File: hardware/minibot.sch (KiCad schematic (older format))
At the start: 36 parts, among them J1 USB_OTG, J2 SWD, J3 RESET, J4 BAUD, J5 CONN_01X18, SW1 BOOT, SW2 RESET, U1 TLV70233DBV, U6 RN41, U7 LSM6DS3US

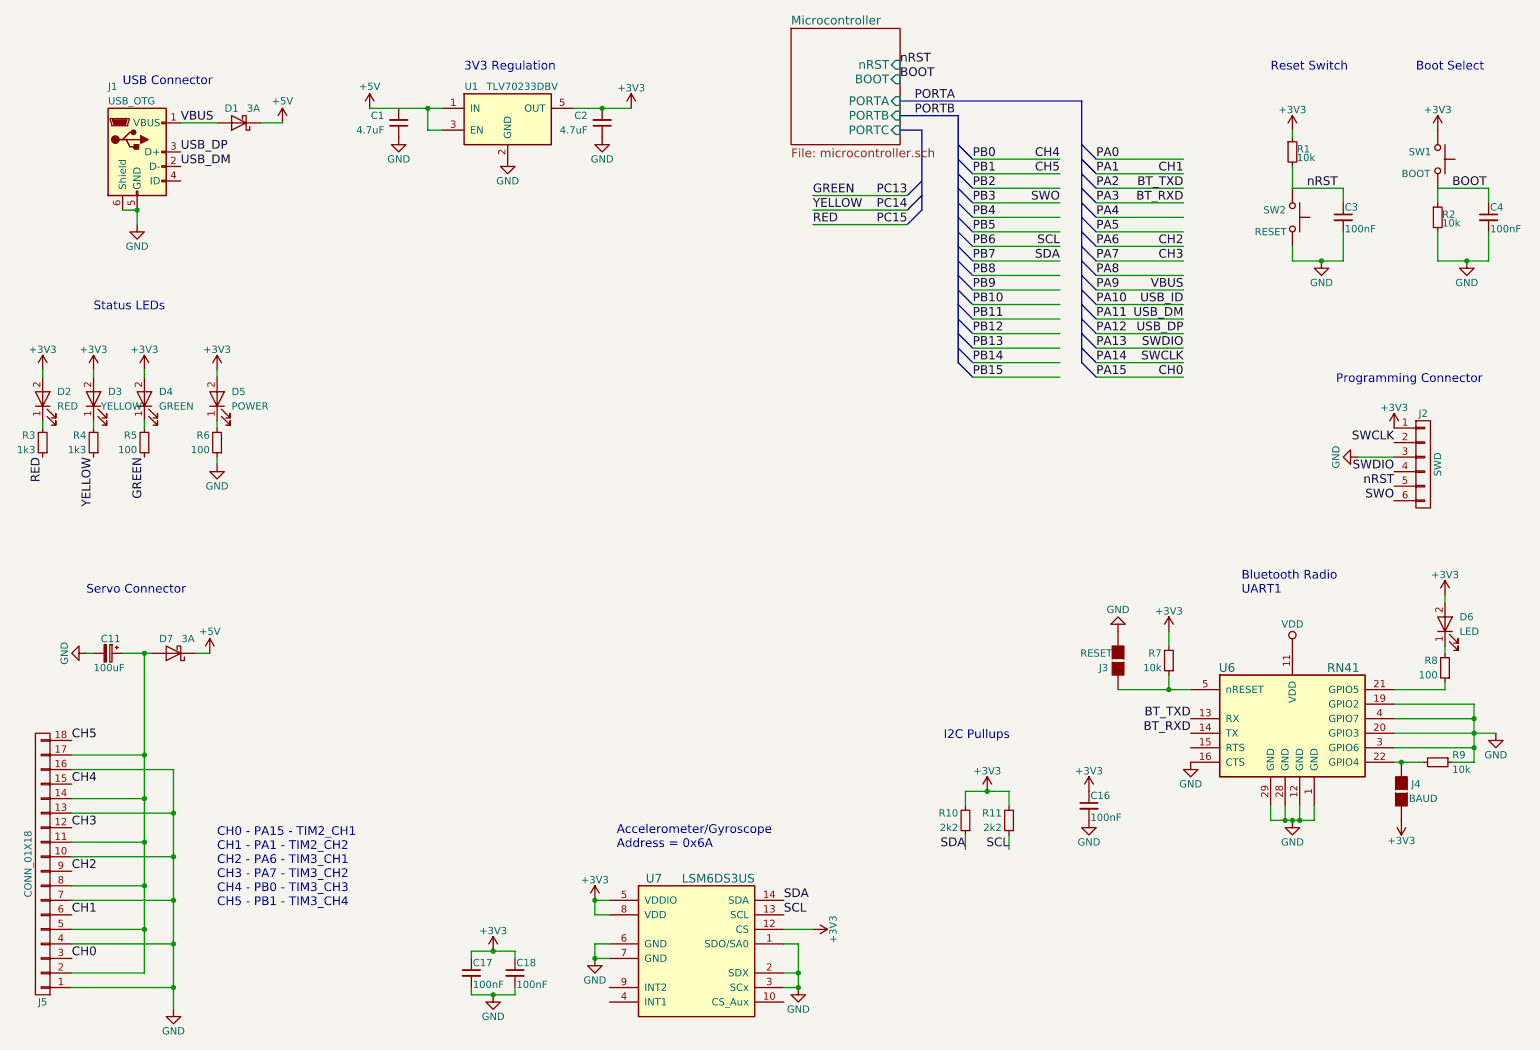
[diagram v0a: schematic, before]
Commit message: Start laying out the components for the PCB
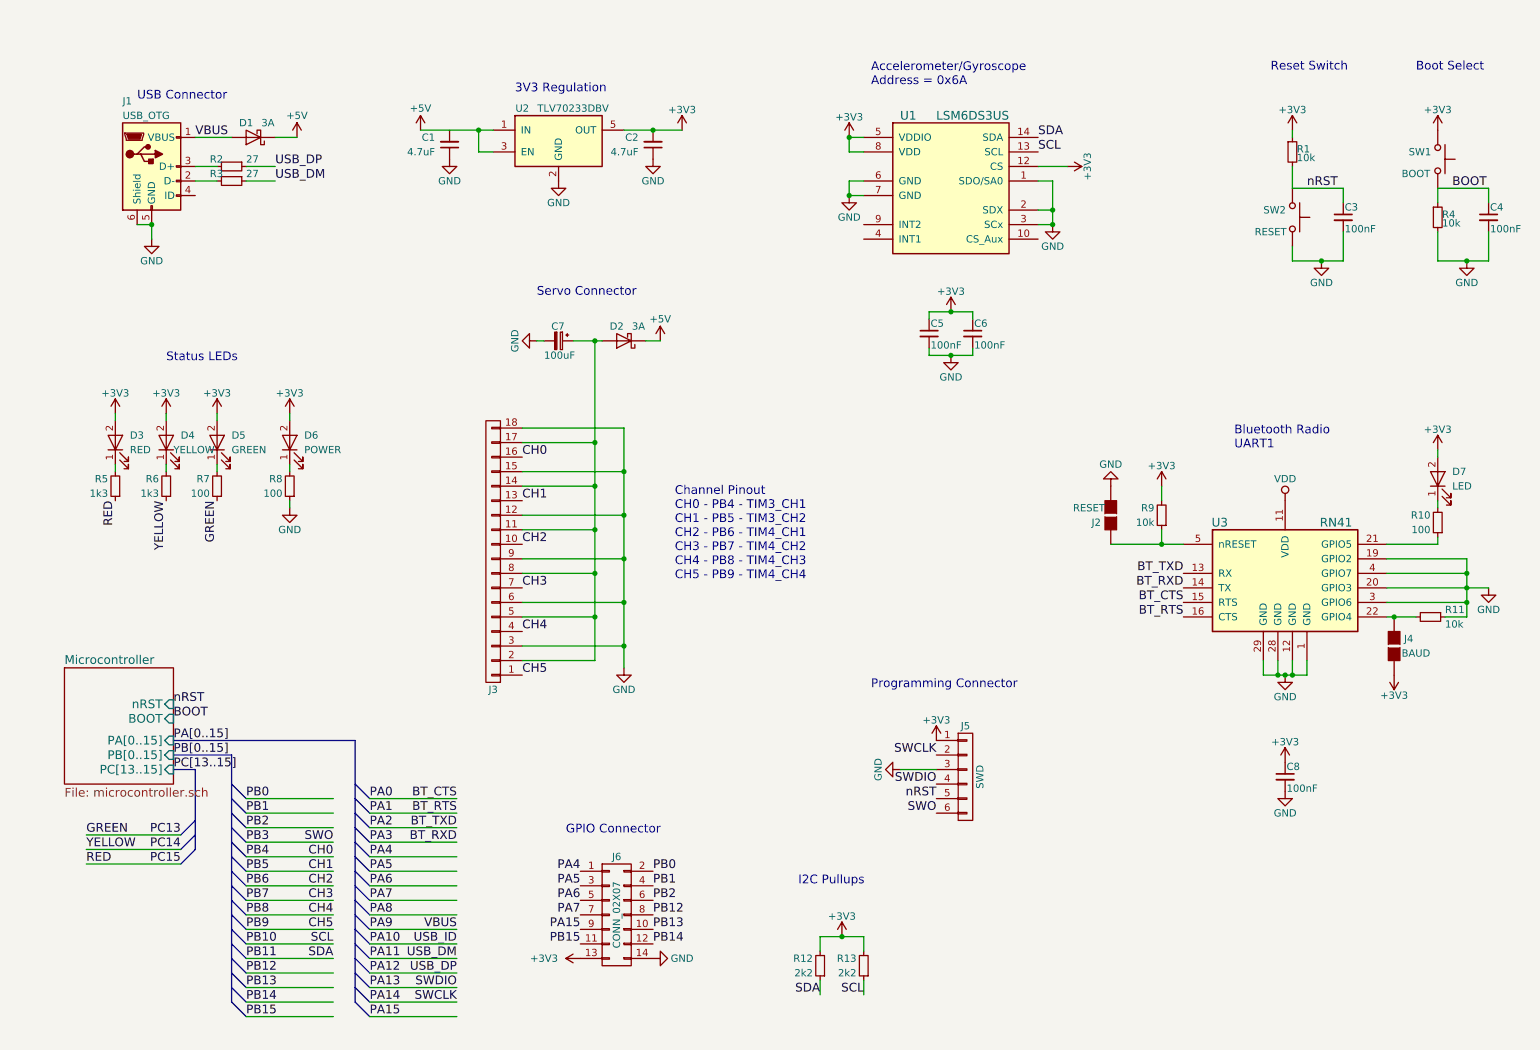
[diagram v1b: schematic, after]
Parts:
- added J6: CONN_02X07, Pin_Headers:Pin_Header_Straight_2x07_Pitch1.27mm, symbol CONN_02X07
- added R2, R3: 27, Resistors_SMD:R_0603, symbol R_Small
- J3: renamed from J5; footprint (none) -> modules:Pin_Header_Angled_3x06_Pitch2.54mm
- J5: renamed from J2; footprint Pin_Headers:Pin_Header_Angled_1x06_Pitch1.27mm -> Pin_Headers:Pin_Header_Straight_1x06_Pitch1.27mm
- SW1, SW2: footprint (none) -> Buttons_Switches_SMD:Panasonic_EVQPUK_EVQPUB
- U1: renamed from U7; footprint (none) -> modules:LSM6DS3US
- U3: renamed from U6; footprint (none) -> modules:RN41
- renumbered C17 to C5, C18 to C6, C11 to C7, C16 to C8, D7 to D2, D2 to D3, D3 to D4, D4 to D5, D5 to D6, D6 to D7, J3 to J2, R8 to R10, R9 to R11, R10 to R12, R11 to R13, R2 to R4, R3 to R5, R4 to R6, R5 to R7, R6 to R8, R7 to R9, U1 to U2
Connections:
- net labels added: BT_CTS, BT_RTS, PA[0..15], PB[0..15], PC[13..15]
- net labels removed: PORTA, PORTB
- wire segments 125 -> 129
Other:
- note added: "Channel Pinout\nCH0 - PB4 - TIM3_CH1\nCH1 - PB5 - TIM3_CH2\nCH2 - PB6 - TIM4_CH1\nCH3 - PB7 - TIM4_CH2\nCH4 - PB8 - TIM4_CH3\nCH5 - PB9 - TIM4_CH4"
- note added: "GPIO Connector\n"
- note removed: "CH0 - PA15 - TIM2_CH1\nCH1 - PA1 - TIM2_CH2\nCH2 - PA6 - TIM3_CH1\nCH3 - PA7 - TIM3_CH2\nCH4 - PB0 - TIM3_CH3\nCH5 - PB1 - TIM3_CH4"
- moved on the sheet: C1, C2, C5, C6, C7, C8, D1, D2, D3, D4, D5, D6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

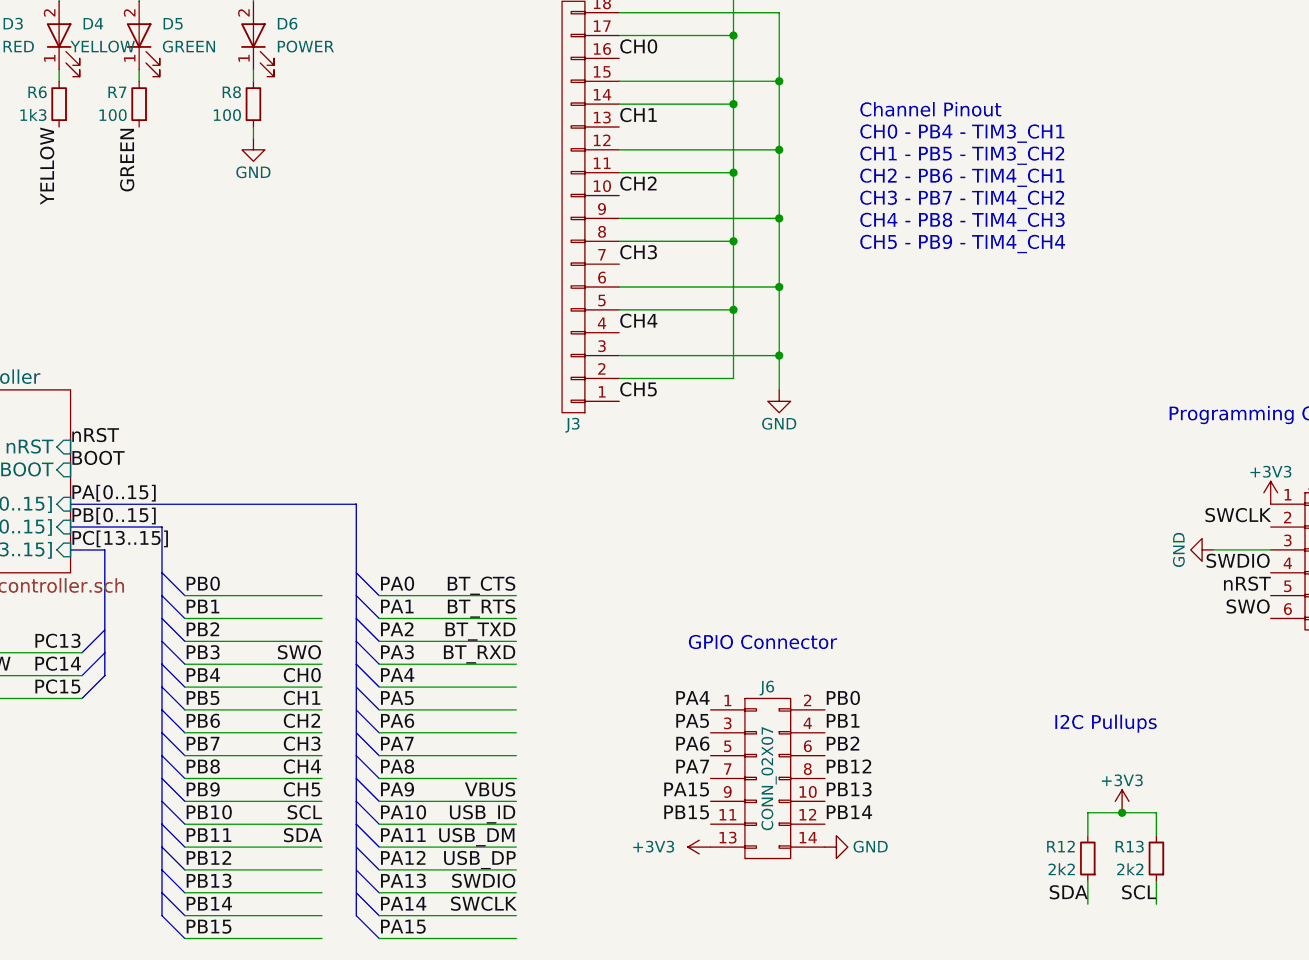
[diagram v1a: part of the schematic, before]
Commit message: Modify the schematic and PCB. At this stage the pinout should be considered and very careful selection of which peripheral goes where needs to be done.
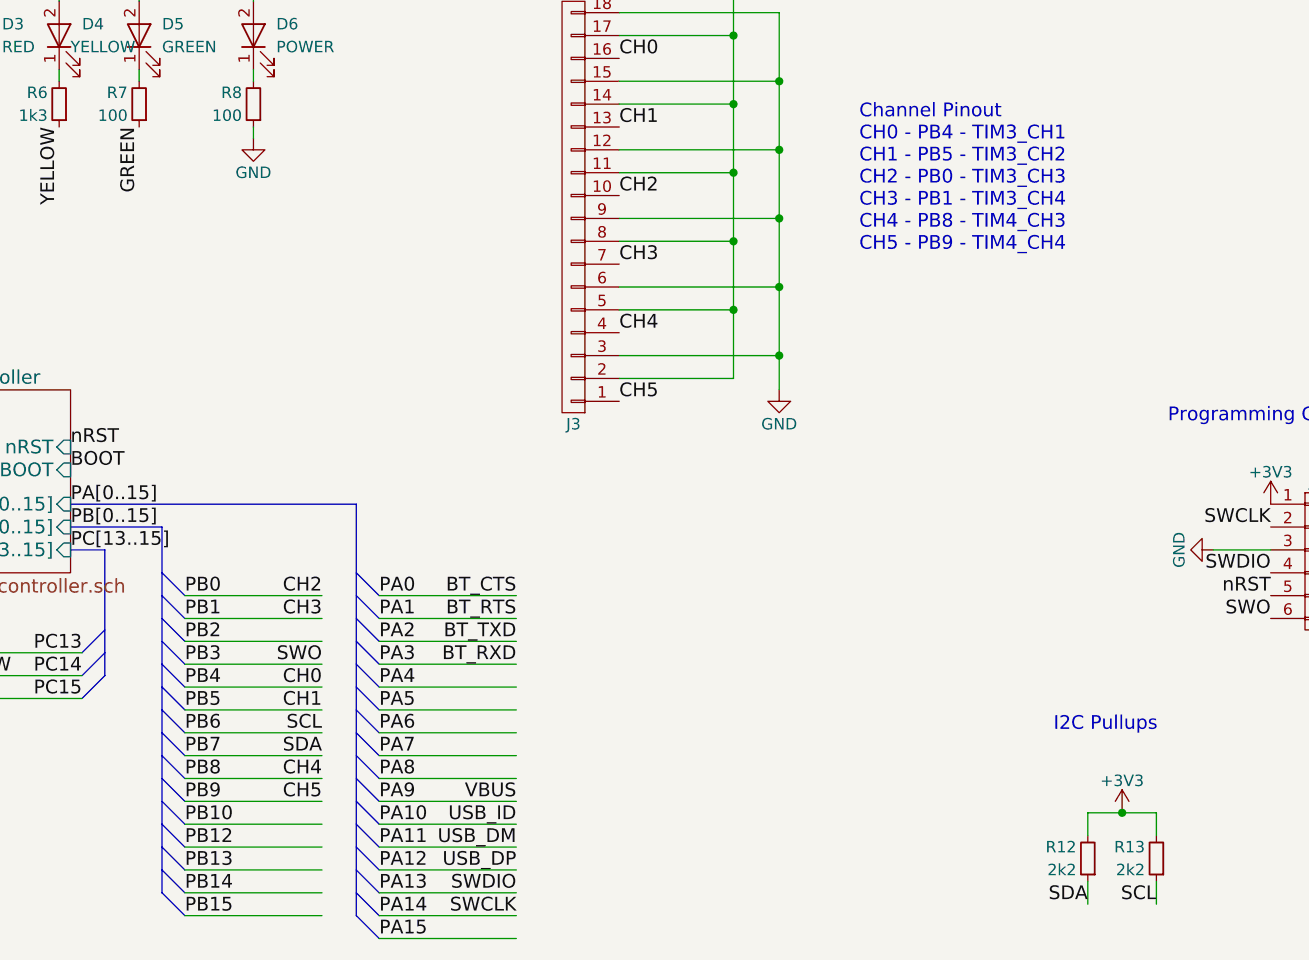
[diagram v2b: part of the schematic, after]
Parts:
- removed J6: CONN_02X07, Pin_Headers:Pin_Header_Straight_2x07_Pitch1.27mm, symbol CONN_02X07
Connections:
- net labels removed: PB11
- wire segments 129 -> 128
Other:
- note added: "Channel Pinout\nCH0 - PB4 - TIM3_CH1\nCH1 - PB5 - TIM3_CH2\nCH2 - PB0 - TIM3_CH3\nCH3 - PB1 - TIM3_CH4\nCH4 - PB8 - TIM4_CH3\nCH5 - PB9 - TIM4_CH4"
- note removed: "Channel Pinout\nCH0 - PB4 - TIM3_CH1\nCH1 - PB5 - TIM3_CH2\nCH2 - PB6 - TIM4_CH1\nCH3 - PB7 - TIM4_CH2\nCH4 - PB8 - TIM4_CH3\nCH5 - PB9 - TIM4_CH4"
- note removed: "GPIO Connector\n"
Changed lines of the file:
@@
 PB10
 Text Label 2250 7050 0    60   ~ 0
-PB11
+PB12
 Text Label 2250 7150 0    60   ~ 0
-PB12
+PB13
 Text Label 2250 7250 0    60   ~ 0
-PB13
-Text Label 2250 7350 0    60   ~ 0
 PB14
-Text Label 2250 7450 0    60   ~ 0
-PB15
 Entry Bus Bus
 	2150 5850 2250 5950
@@
 Entry Bus Bus
 	2150 7250 2250 7350
-Entry Bus Bus
-	2150 7350 2250 7450
 Entry Bus Bus
 	3000 5850 3100 5950
@@
 Text Label 2850 6450 2    60   ~ 0
 CH1
-Text Label 2850 6550 2    60   ~ 0
+Text Label 2850 5950 2    60   ~ 0
 CH2
-Text Label 2850 6650 2    60   ~ 0
+Text Label 2850 6050 2    60   ~ 0
 CH3
 Text Label 2850 6750 2    60   ~ 0
@@
 Wire Bus Line
 	1750 5650 2150 5650
-Wire Bus Line
-	2150 5650 2150 7350
 Wire Wire Line
 	1350 3700 1350 3650
@@
 Wire Wire Line
 	2250 7350 2850 7350
-Wire Wire Line
-	2250 7450 2850 7450
 Wire Wire Line
 	3700 5950 3100 5950
@@
 Text Notes 6550 1050 0    60   ~ 0
 Accelerometer/Gyroscope\nAddress = 0x6A\n
-Text Label 2850 6950 2    60   ~ 0
+Text Label 2850 6550 2    60   ~ 0
 SCL
-Text Label 2850 7050 2    60   ~ 0
+Text Label 2850 6650 2    60   ~ 0
 SDA
 Text Label 6200 7300 2    60   ~ 0
@@
 	3450 1350 3950 1350
 Text Notes 5200 4450 0    60   ~ 0
-Channel Pinout\nCH0 - PB4 - TIM3_CH1\nCH1 - PB5 - TIM3_CH2\nCH2 - PB6 - TIM4_CH1\nCH3 - PB7 - TIM4_CH2\nCH4 - PB8 - TIM4_CH3\nCH5 - PB9 - TIM4_CH4
+Channel Pinout\nCH0 - PB4 - TIM3_CH1\nCH1 - PB5 - TIM3_CH2\nCH2 - PB0 - TIM3_CH3\nCH3 - PB1 - TIM3_CH4\nCH4 - PB8 - TIM4_CH3\nCH5 - PB9 - TIM4_CH4
 $Comp
 L +3V3 #PWR022
@@
 Text Label 3700 6050 2    60   ~ 0
 BT_RTS
-Text Label 5050 6450 0    60   ~ 0
-PB0
-Text Label 5050 6550 0    60   ~ 0
-PB1
-Text Label 5050 6650 0    60   ~ 0
-PB2
-Text Label 5050 6750 0    60   ~ 0
-PB12
-Text Label 5050 6850 0    60   ~ 0
-PB13
-Text Label 5050 6950 0    60   ~ 0
-PB14
-Text Label 4550 6950 2    60   ~ 0
-PB15
-Text Label 4550 6850 2    60   ~ 0
-PA15
-Text Label 4550 6750 2    60   ~ 0
-PA7
-Text Label 4550 6650 2    60   ~ 0
-PA6
-Text Label 4550 6550 2    60   ~ 0
-PA5
-Text Label 4550 6450 2    60   ~ 0
-PA4
-$Comp
-L CONN_02X07 J6
-U 1 1 594DF77C
-P 4800 6750
-F 0 "J6" H 4800 7150 50  0000 C CNN
-F 1 "CONN_02X07" V 4800 6750 50  0000 C CNN
-F 2 "Pin_Headers:Pin_Header_Straight_2x07_Pitch1.27mm" H 4800 5550 50  0001 C CNN
-F 3 "" H 4800 5550 50  0001 C CNN
-	1    4800 6750
-	1    0    0    -1
-$EndComp
-$Comp
-L +3V3 #PWR038
-U 1 1 594DFEF4
-P 4550 7050
-F 0 "#PWR038" H 4550 6900 50  0001 C CNN
-F 1 "+3V3" V 4550 7300 50  0000 C CNN
-F 2 "" H 4550 7050 50  0001 C CNN
-F 3 "" H 4550 7050 50  0001 C CNN
-	1    4550 7050
-	0    -1   -1   0
-$EndComp
-$Comp
-L GND #PWR039
-U 1 1 594E080C
-P 5050 7050
-F 0 "#PWR039" H 5050 6800 50  0001 C CNN
-F 1 "GND" V 5050 6850 50  0000 C CNN
-F 2 "" H 5050 7050 50  0001 C CNN
-F 3 "" H 5050 7050 50  0001 C CNN
-	1    5050 7050
-	0    -1   -1   0
-$EndComp
-Text Notes 4450 6200 0    60   ~ 0
-GPIO Connector\n
 Text Label 1750 5550 0    60   ~ 0
 PA[0..15]
@@
 Wire Wire Line
 	2250 1700 2450 1700
+Wire Bus Line
+	2150 5650 2150 7250
+Text Label 2250 7350 0    60   ~ 0
+PB15
 $EndSCHEMATC
